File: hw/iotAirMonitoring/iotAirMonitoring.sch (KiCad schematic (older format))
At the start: 0 parts

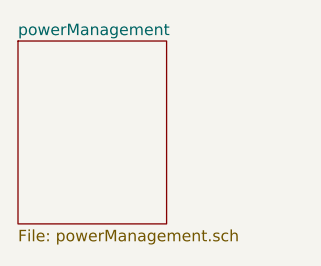
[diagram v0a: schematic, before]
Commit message: Finish stepdown schematic
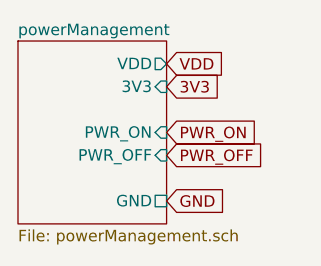
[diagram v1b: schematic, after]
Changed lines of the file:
@@
 F0 "powerManagement" 50
 F1 "powerManagement.sch" 50
+F2 "GND" U R 2550 2450 50
+F3 "3V3" I R 2550 1950 50
+F4 "PWR_ON" I R 2550 2150 50
+F5 "PWR_OFF" I R 2550 2250 50
+F6 "VDD" O R 2550 1850 50
 $EndSheet
+Text GLabel 2550 1850 2    50   Input ~ 0
+VDD
+Text GLabel 2550 1950 2    50   Input ~ 0
+3V3
+Text GLabel 2550 2150 2    50   Input ~ 0
+PWR_ON
+Text GLabel 2550 2250 2    50   Input ~ 0
+PWR_OFF
+Text GLabel 2550 2450 2    50   Input ~ 0
+GND
 $EndSCHEMATC

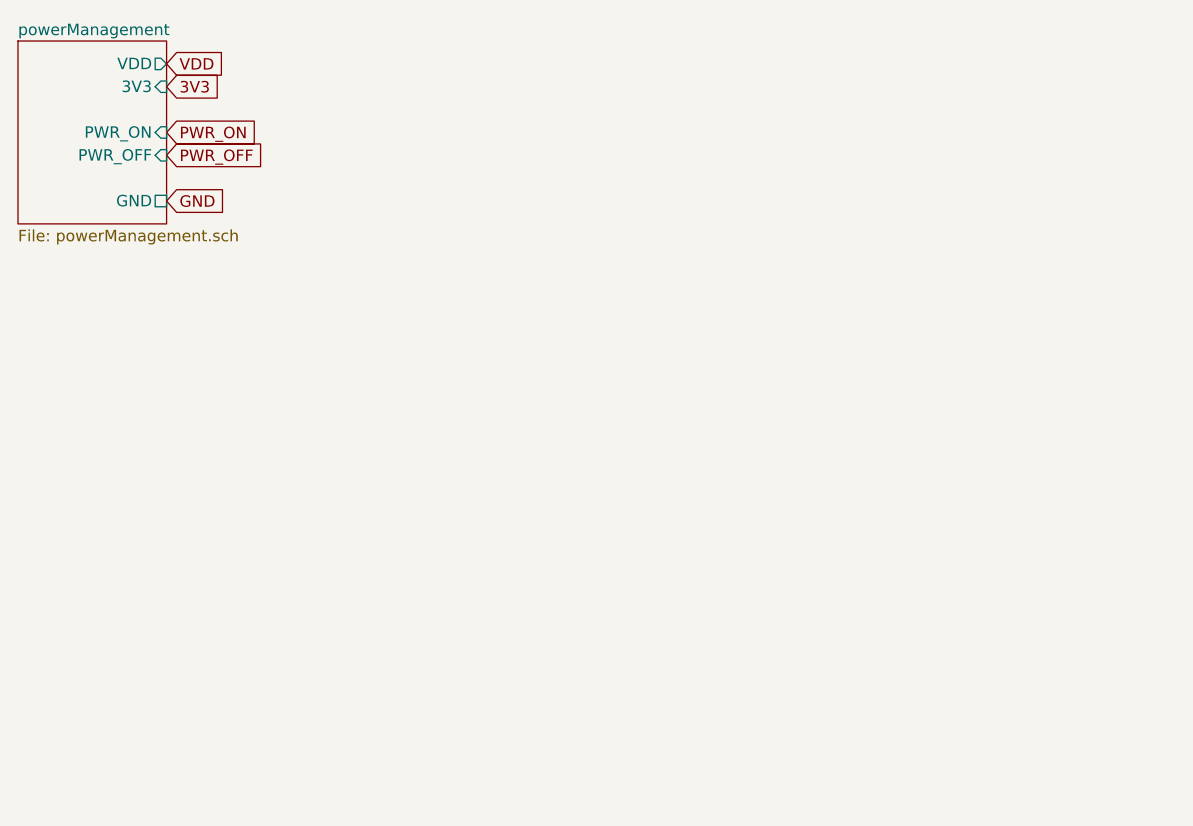
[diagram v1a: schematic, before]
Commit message: Add LDO regulator and ESP32
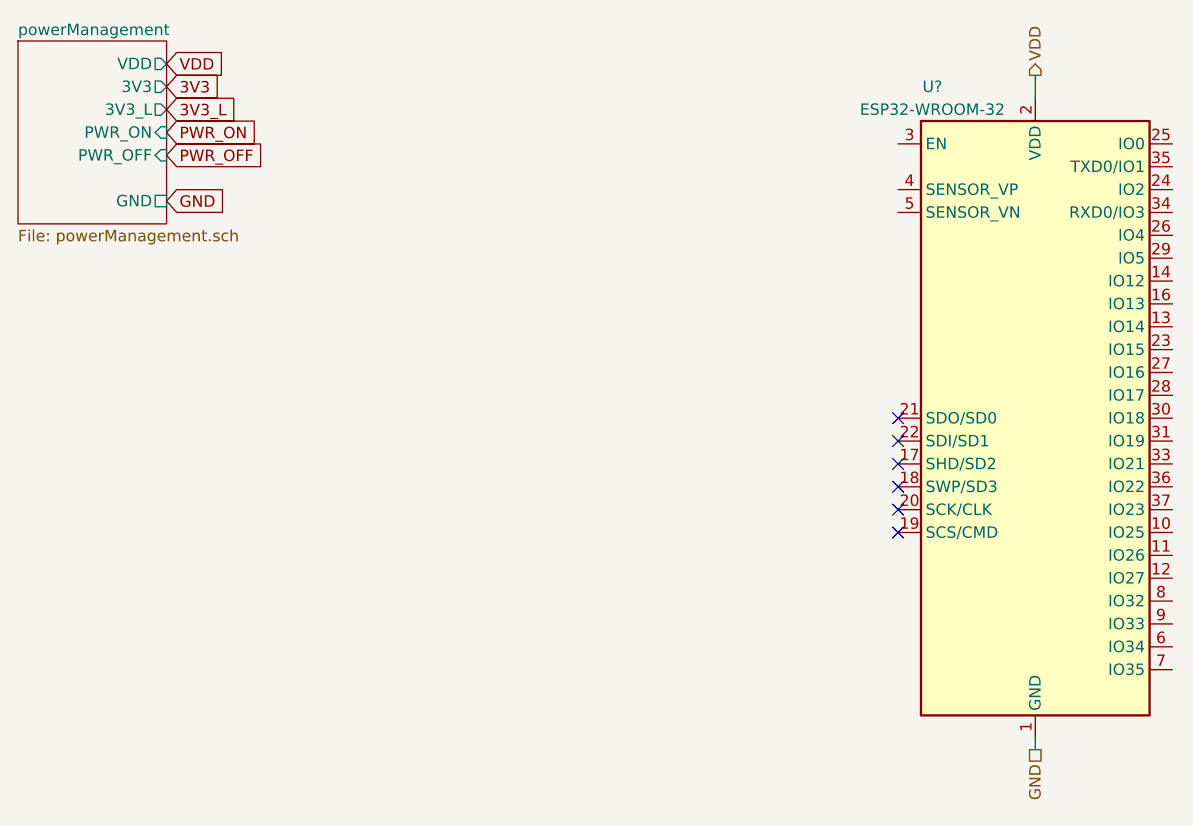
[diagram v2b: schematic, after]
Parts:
- added U?: ESP32-WROOM-32, RF_Module:ESP32-WROOM-32, symbol RF_Module:ESP32-WROOM-32
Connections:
- net GND: now also U?.1 (GND), U?.15 (GND), U?.38 (GND), U?.39 (GND)
- net VDD: now also U?.2 (VDD)
- no-connect marks 0 -> 6
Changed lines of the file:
@@
 F1 "powerManagement.sch" 50
 F2 "GND" U R 2550 2450 50
-F3 "3V3" I R 2550 1950 50
-F4 "PWR_ON" I R 2550 2150 50
-F5 "PWR_OFF" I R 2550 2250 50
-F6 "VDD" O R 2550 1850 50
+F3 "PWR_ON" I R 2550 2150 50
+F4 "PWR_OFF" I R 2550 2250 50
+F5 "VDD" O R 2550 1850 50
+F6 "3V3_L" O R 2550 2050 50
+F7 "3V3" O R 2550 1950 50
 $EndSheet
 Text GLabel 2550 1850 2    50   Input ~ 0
@@
 Text GLabel 2550 2450 2    50   Input ~ 0
 GND
+Text GLabel 2550 2050 2    50   Input ~ 0
+3V3_L
+$Comp
+L RF_Module:ESP32-WROOM-32 U?
+U 1 1 6179D141
+P 6350 3400
+F 0 "U?" H 5900 4850 50  0000 C CNN
+F 1 "ESP32-WROOM-32" H 5900 4750 50  0000 C CNN
+F 2 "RF_Module:ESP32-WROOM-32" H 6350 1900 50  0001 C CNN
+F 3 "https://www.espressif.com/sites/default/files/documentation/esp32-wroom-32_datasheet_en.pdf" H 6050 3450 50  0001 C CNN
+F 4 "C82899" H 6350 3400 50  0001 C CNN "LCSC"
+	1    6350 3400
+	1    0    0    -1
+$EndComp
+Text HLabel 6350 4850 3    50   UnSpc ~ 0
+GND
+Wire Wire Line
+	6350 4850 6350 4800
+NoConn ~ 5750 3400
+NoConn ~ 5750 3500
+NoConn ~ 5750 3600
+NoConn ~ 5750 3700
+NoConn ~ 5750 3800
+NoConn ~ 5750 3900
+Text HLabel 6350 1900 1    50   Output ~ 0
+VDD
+Wire Wire Line
+	6350 1900 6350 2000
 $EndSCHEMATC

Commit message: More work on schematic
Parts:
- added C14: 22u, Capacitor_SMD:C_0805_2012Metric, symbol Device:C
- added C15, C16: 100n, Capacitor_SMD:C_0402_1005Metric, symbol Device:C
- added R10, R11: 3k3, symbol Device:R
- added SW1, SW2: SW_Push, symbol Switch:SW_Push
- added TP1: TP_SDA, TestPoint:TestPoint_Pad_D1.5mm, symbol Connector:TestPoint
- added TP2: TP_SCL, TestPoint:TestPoint_Pad_D1.5mm, symbol Connector:TestPoint
- gave numbers to parts that had none: 1
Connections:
- net GND: now also C14.2, C15.2, C16.2, SW1.2, SW2.2
- net PWR_OFF: now also C16.1, SW2.1
- net PWR_ON: now also C15.1, SW1.1
- net VDD: now also C14.1, R10.1, R11.2
- net RX: now reaches U3.24 (IO2)
- net SDA: now reaches U3.33 (IO21)
- net SDA: now also R10.2, TP1.1
- net TX: now reaches U3.35 (TXD0/IO1)
- net SCL: now reaches U3.36 (IO22)
- net SCL: now also R11.1, TP2.1
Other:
- note added: "UNUSABLE\n(FLASH MEMORY)"
- moved on the sheet: U3

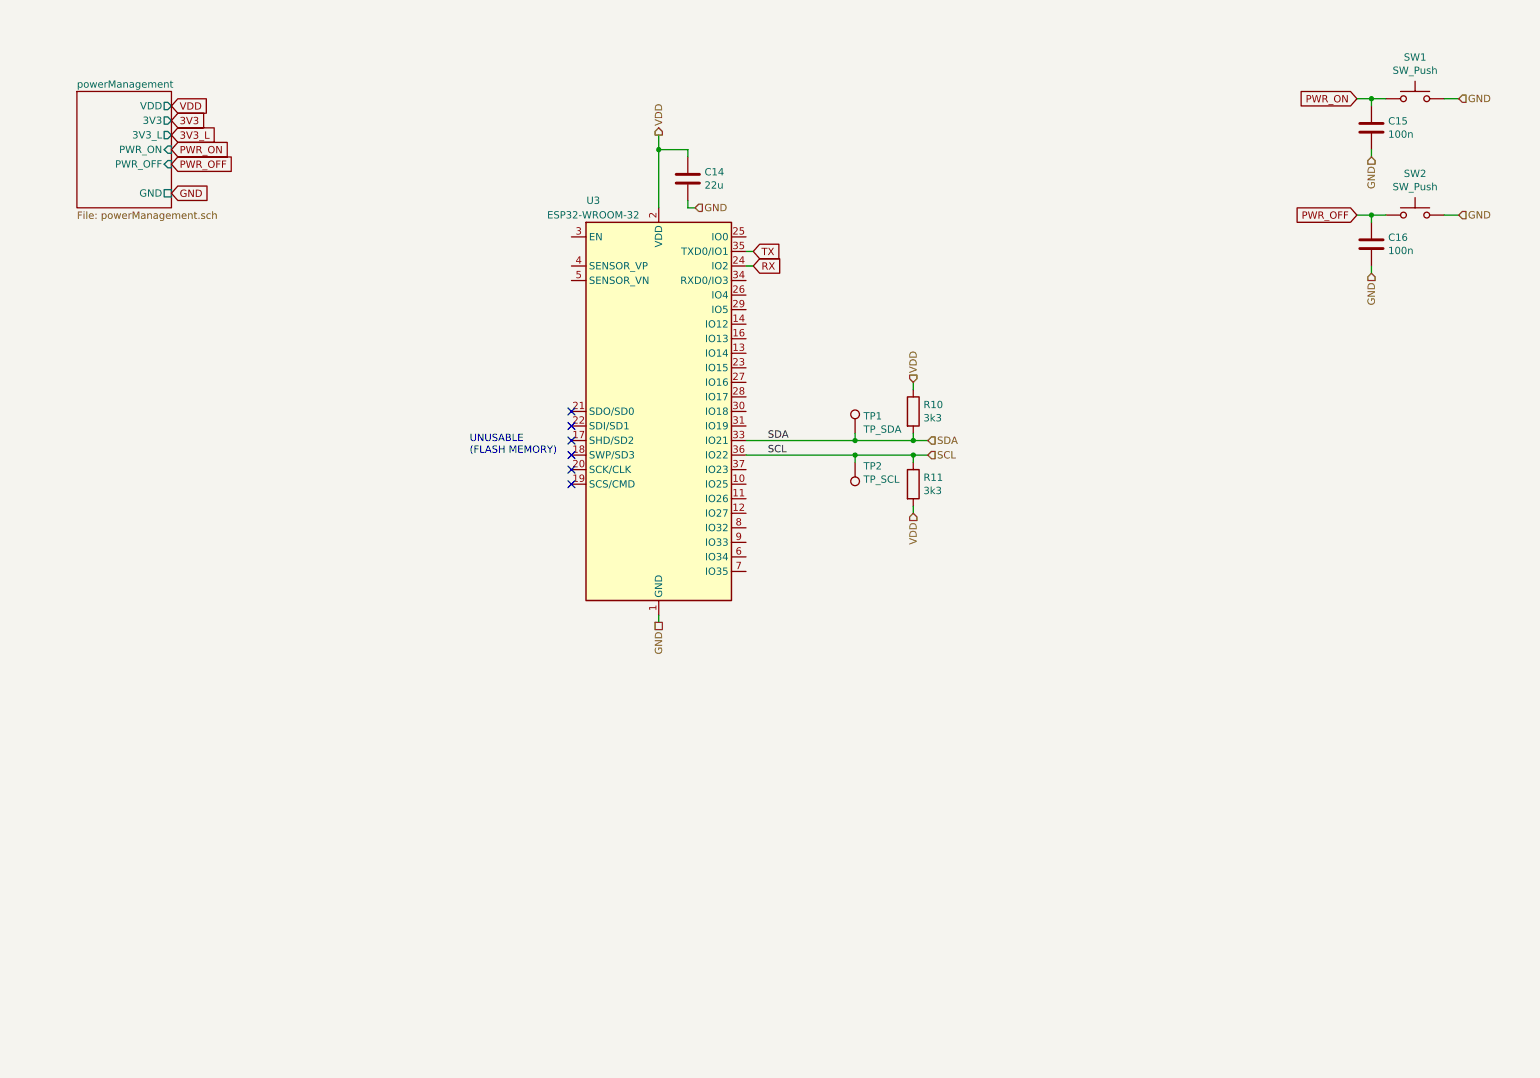
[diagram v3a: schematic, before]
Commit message: Add way more parts to schematic
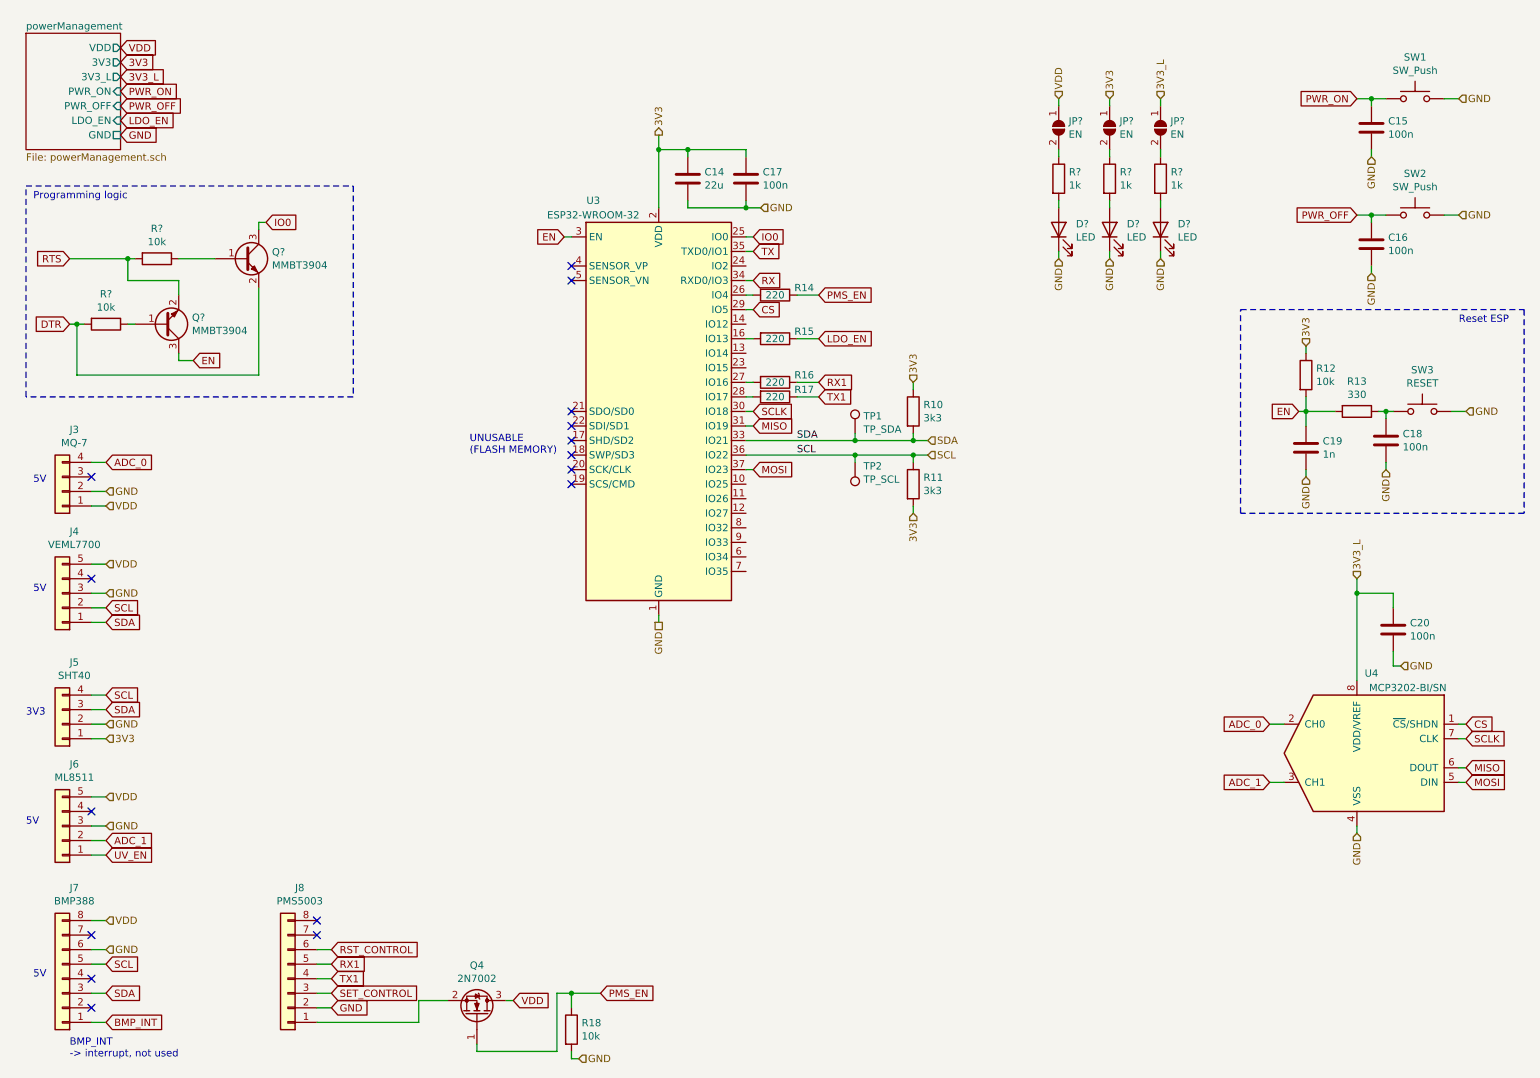
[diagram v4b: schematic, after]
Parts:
- added C17, C18, C20: 100n, Capacitor_SMD:C_0402_1005Metric, symbol Device:C
- added C19: 1n, symbol Device:C
- added D? (x3): LED, symbol Device:LED
- added J3: MQ-7, Connector_PinSocket_2.54mm:PinSocket_1x04_P2.54mm_Vertical, symbol Connector_Generic:Conn_01x04
- added J4: VEML7700, Connector_PinSocket_2.54mm:PinSocket_1x05_P2.54mm_Vertical, symbol Connector_Generic:Conn_01x05
- added J5: SHT40, Connector_PinSocket_2.54mm:PinSocket_1x04_P2.54mm_Vertical, symbol Connector_Generic:Conn_01x04
- added J6: ML8511, Connector_PinSocket_2.54mm:PinSocket_1x05_P2.54mm_Vertical, symbol Connector_Generic:Conn_01x05
- added J7: BMP388, Connector_PinSocket_2.54mm:PinSocket_1x08_P2.54mm_Vertical, symbol Connector_Generic:Conn_01x08
- added J8: PMS5003, symbol Connector_Generic:Conn_01x08
- added JP? (x3): EN, Jumper:SolderJumper-2_P1.3mm_Open_RoundedPad1.0x1.5mm, symbol Jumper:SolderJumper_2_Open
- added Q4: 2N7002, Package_TO_SOT_SMD:SOT-23, symbol Transistor_FET:2N7002
- added Q? (x2): MMBT3904, Package_TO_SOT_SMD:SOT-23, symbol Device:Q_NPN_BEC
- added R12, R18, R? (x2): 10k, Resistor_SMD:R_0402_1005Metric, symbol Device:R
- added R13: 330, Resistor_SMD:R_0402_1005Metric, symbol Device:R
- added R14, R15, R16, R17: 220, Resistor_SMD:R_0402_1005Metric, symbol Device:R
- added R? (x3): 1k, Resistor_SMD:R_0402_1005Metric, symbol Device:R
- added SW3: RESET, symbol Switch:SW_Push
- added U4: MCP3202-BI/SN, Package_SO:SOIC-8_3.9x4.9mm_P1.27mm, symbol Analog_ADC:MCP3202
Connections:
- net 3V3: now also C14.1, R10.1, R11.2, U3.2 (VDD), C17.1, J5.1 (Pin_1), JP?.1 (A), R12.1
- net 3V3_L: now also C20.1, JP?.1 (A), U4.8 (VDD/VREF)
- net GND: now also C17.2, C18.2, C19.2, C20.2, D?.1 (K), D?.1 (K), D?.1 (K), J3.2 (Pin_2), J4.3 (Pin_3), J5.2 (Pin_2), J6.3 (Pin_3), J7.6 (Pin_6), J8.2 (Pin_2), R18.2, SW3.2, U4.4 (VSS)
- net RX: now also U3.34 (RXD0/IO3); no longer U3.24 (IO2)
- net SCL: now also J4.2 (Pin_2), J5.4 (Pin_4), J7.5 (Pin_5)
- net SDA: now also J4.1 (Pin_1), J5.3 (Pin_3), J7.3 (Pin_3)
- net VDD: now also J3.1 (Pin_1), J4.5 (Pin_5), J6.5 (Pin_5), J7.8 (Pin_8), JP?.1 (A), Q4.3 (D); no longer C14.1, R10.1, R11.2, U3.2 (VDD)
- net at U3.16 (IO13): now also R15.2
- net IO0: now reaches U3.25 (IO0)
- net IO0: now also Q?.3 (C)
- net at U3.26 (IO4): now also R14.2
- net at U3.27 (IO16): now also R16.2
- net at U3.28 (IO17): now also R17.2
- net CS: now reaches U3.29 (IO5)
- net CS: now also U4.1 (~CS~/SHDN)
- net EN: now reaches U3.3 (EN)
- net EN: now also C19.1, Q?.3 (C), R12.2, R13.2
- net SCLK: now reaches U3.30 (IO18)
- net SCLK: now also U4.7 (CLK)
- net MISO: now reaches U3.31 (IO19)
- net MISO: now also U4.6 (DOUT)
- net MOSI: now reaches U3.37 (IO23)
- net MOSI: now also U4.5 (DIN)
- new net: C18.1, R13.1, SW3.1
- new net: J8.1 (Pin_1), Q4.2 (S)
- new net: D?.2 (A), R?.2 (x3)
- new net: JP?.2 (B), R?.1 (x3)
- new net: Q?.1 (B), R?.1 (x2)
- new net ADC_0: J3.4 (Pin_4), U4.2 (CH0)
- new net ADC_1: J6.2 (Pin_2), U4.3 (CH1)
- new net BMP_INT: J7.1 (Pin_1)
- new net DTR: Q?.2 (E), R?.2
- new net LDO_EN: R15.1
- new net PMS_EN: Q4.1 (G), R14.1, R18.1
- new net RST_CONTROL: J8.6 (Pin_6)
- new net RTS: Q?.2 (E), R?.2
- new net RX1: J8.5 (Pin_5), R16.1
- new net SET_CONTROL: J8.3 (Pin_3)
- new net TX1: J8.4 (Pin_4), R17.1
- new net UV_EN: J6.1 (Pin_1)
- no-connect marks 6 -> 16
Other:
- note added: "3V3"
- note added: "5V"
- note added: "BMP_INT\n-> interrupt, not used"
- note added: "Programming logic"
- note added: "Reset ESP"

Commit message: Schematic nearly finished
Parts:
- added C7: 100n, Capacitor_SMD:C_0402_1005Metric, symbol Device:C
- added D4: LED, LED_SMD:LED_0805_2012Metric_Pad1.15x1.40mm_HandSolder, symbol Device:LED
- added H1, H2, H3, H4: MountingHole, MountingHole:MountingHole_3.2mm_M3_Pad_Via, symbol Mechanical:MountingHole
- added J4: PROGRAMMER, Connector_PinHeader_2.54mm:PinHeader_1x06_P2.54mm_Vertical, symbol Connector_Generic:Conn_01x06
- added J6: EN_3V3_PROGRAMMER, Connector_PinHeader_2.54mm:PinHeader_1x02_P2.54mm_Vertical, symbol Connector_Generic:Conn_01x02
- added Q3, Q5, Q7: AO3401A, Package_TO_SOT_SMD:SOT-23, symbol Device:Q_PMOS_GSD
- added Q4, Q6: 2N7002, Package_TO_SOT_SMD:SOT-23, symbol Transistor_FET:2N7002
- added R1, R2, R21: R, Resistor_SMD:R_0805_2012Metric_Pad1.20x1.40mm_HandSolder, symbol Device:R
- added R13, R17, R20, R22, R24, R25, R26: 100k, Resistor_SMD:R_0402_1005Metric, symbol Device:R
- added R19, R23: 220, Resistor_SMD:R_0402_1005Metric, symbol Device:R
- added SW4: SW_Push, Button_Switch_THT:SW_PUSH_6mm, symbol Switch:SW_Push
- C6: renamed from C19; footprint (none) -> Capacitor_SMD:C_0402_1005Metric; LCSC (none) -> C1523
- D1, D2, D3: renamed from D?; footprint (none) -> LED_SMD:LED_0805_2012Metric_Pad1.15x1.40mm_HandSolder
- R14: renamed from R10; footprint (none) -> Resistor_SMD:R_0402_1005Metric; LCSC (none) -> C25890
- R16: renamed from R11; footprint (none) -> Resistor_SMD:R_0402_1005Metric; LCSC (none) -> C25890
- R18: value 10k -> 220; LCSC C25744 -> C25091
- SW1, SW2, SW3: footprint (none) -> Button_Switch_THT:SW_PUSH_6mm
- gave numbers to parts that had none: 10
- renumbered C15 to C1, C14 to C2, C17 to C3, C16 to C4, C18 to C5, C20 to C8, J3 to J1, J4 to J2, J5 to J3, J6 to J5, Q4 to Q8, R12 to R10, R16 to R11, R17 to R12, R13 to R15, R14 to R7, R15 to R9, U3 to U1, U4 to U2
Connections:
- net 3V3: now also J6.1 (Pin_1), R13.1
- net BMP_INT: now also U1.4 (SENSOR_VP)
- net DTR: now also J4.5 (Pin_5)
- net GND: now also Q8.2 (S), C7.2, D4.1 (K), J4.2 (Pin_2), Q4.2 (S), Q6.2 (S), R2.2, R20.2, R24.2, R26.2, SW4.2; no longer R18.2
- net PMS_EN: now also R26.1; no longer R18.1
- net PWR_OFF: now also U1.12 (IO27)
- net RTS: now also J4.6 (Pin_6)
- net RX: now also J4.3 (Pin_3)
- net TX: now also J4.4 (Pin_4)
- net VDD: now also Q3.2 (S), Q5.2 (S), Q7.2 (S), R1.1, R17.1, R22.1, R25.1; no longer J1.1 (Pin_1), J2.5 (Pin_5), J5.5 (Pin_5), J7.8 (Pin_8), Q8.3 (D)
- net SEN_VDD_EN: now reaches U1.10 (IO25)
- net SEN_VDD_EN: now also R23.1
- net MQ_EN: now reaches U1.11 (IO26)
- net MQ_EN: now also R18.1
- net ADC_VIN: now reaches U1.6 (IO34)
- net ADC_VIN: now also R1.2, R2.1
- net at U1.7 (IO35): now also R19.2
- net LED: now reaches U1.8 (IO32)
- net LED: now also R21.1
- net at J8.1 (Pin_1): now also Q7.3 (D); no longer Q8.2 (S)
- new net: Q7.1 (G), Q8.3 (D), R25.2
- new net: Q4.1 (G), R18.2, R20.1
- new net: Q3.1 (G), Q4.3 (D), R17.2
- new net: Q6.1 (G), R23.2, R24.1
- new net: Q5.1 (G), Q6.3 (D), R22.2
- new net: D4.2 (A), R21.2
- new net: J4.1 (Pin_1), J6.2 (Pin_2)
- new net MQ_7-VDD: J1.1 (Pin_1), Q3.3 (D)
- new net SEN_VDD: J2.5 (Pin_5), J5.5 (Pin_5), J7.8 (Pin_8), Q5.3 (D)
- new net SWITCH: C7.1, R13.2, R19.1, SW4.1
- no-connect marks 16 -> 15
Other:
- note added: "5V\n150mA"
- note added: "Optional LED"
- note added: "Optional voltage\ndivider for Vin"
- moved on the sheet: Q8
